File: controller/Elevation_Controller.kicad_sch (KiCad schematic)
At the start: 0 parts

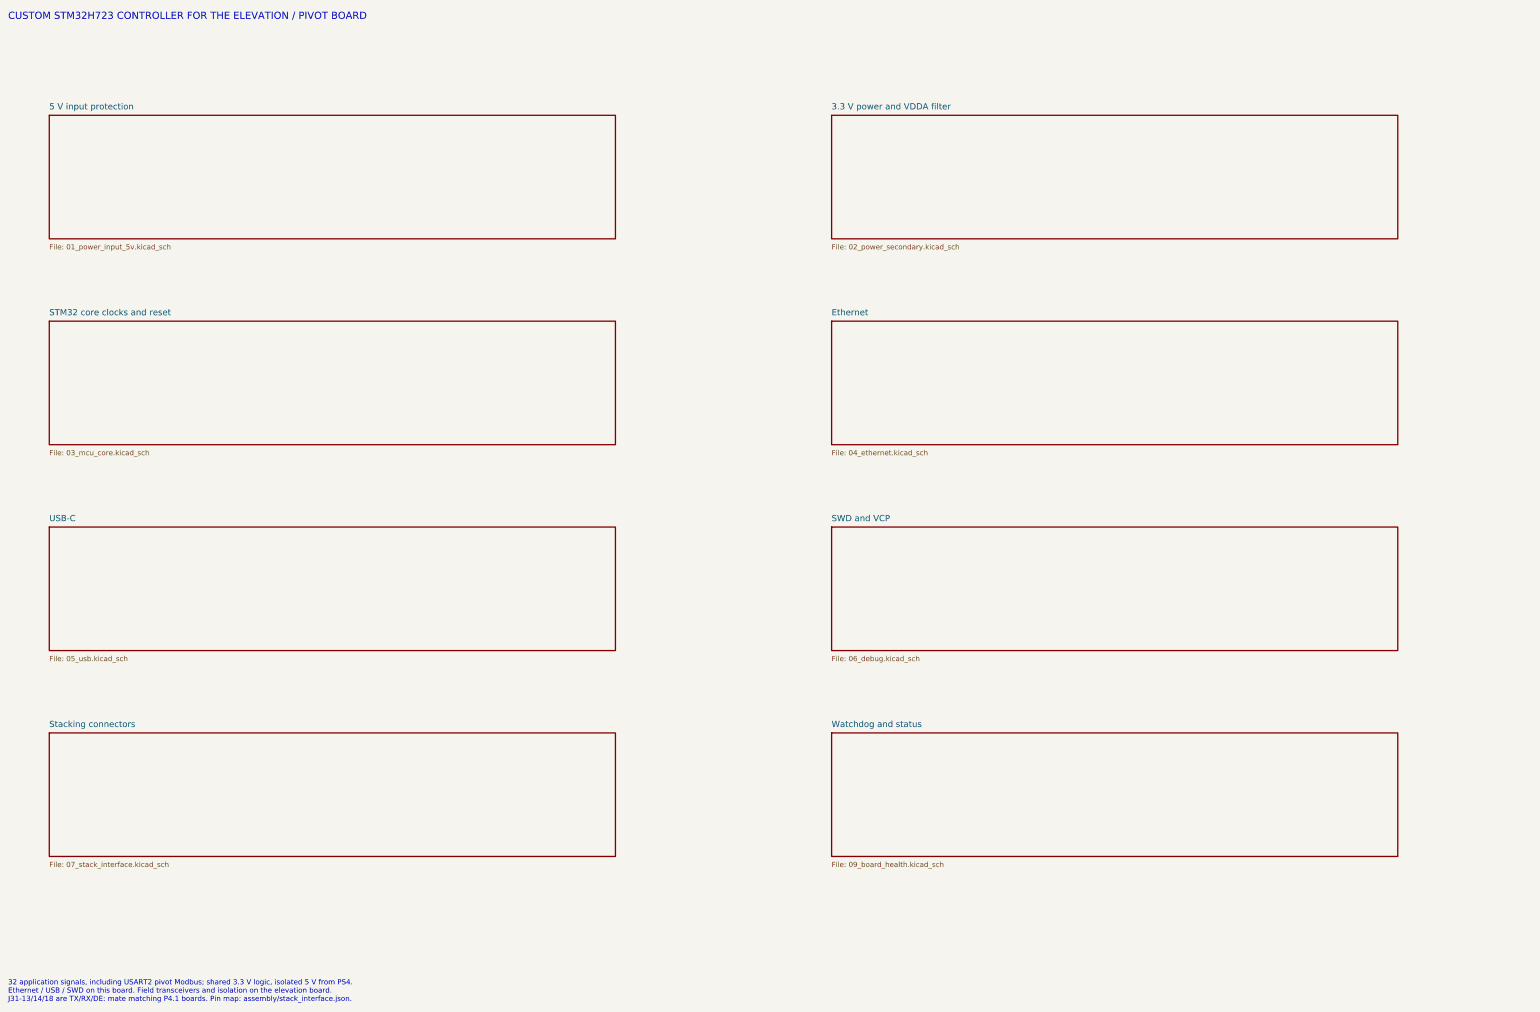
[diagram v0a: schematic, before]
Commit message: Build P6 80x130 stack with redistributed SSI and stepper interfaces
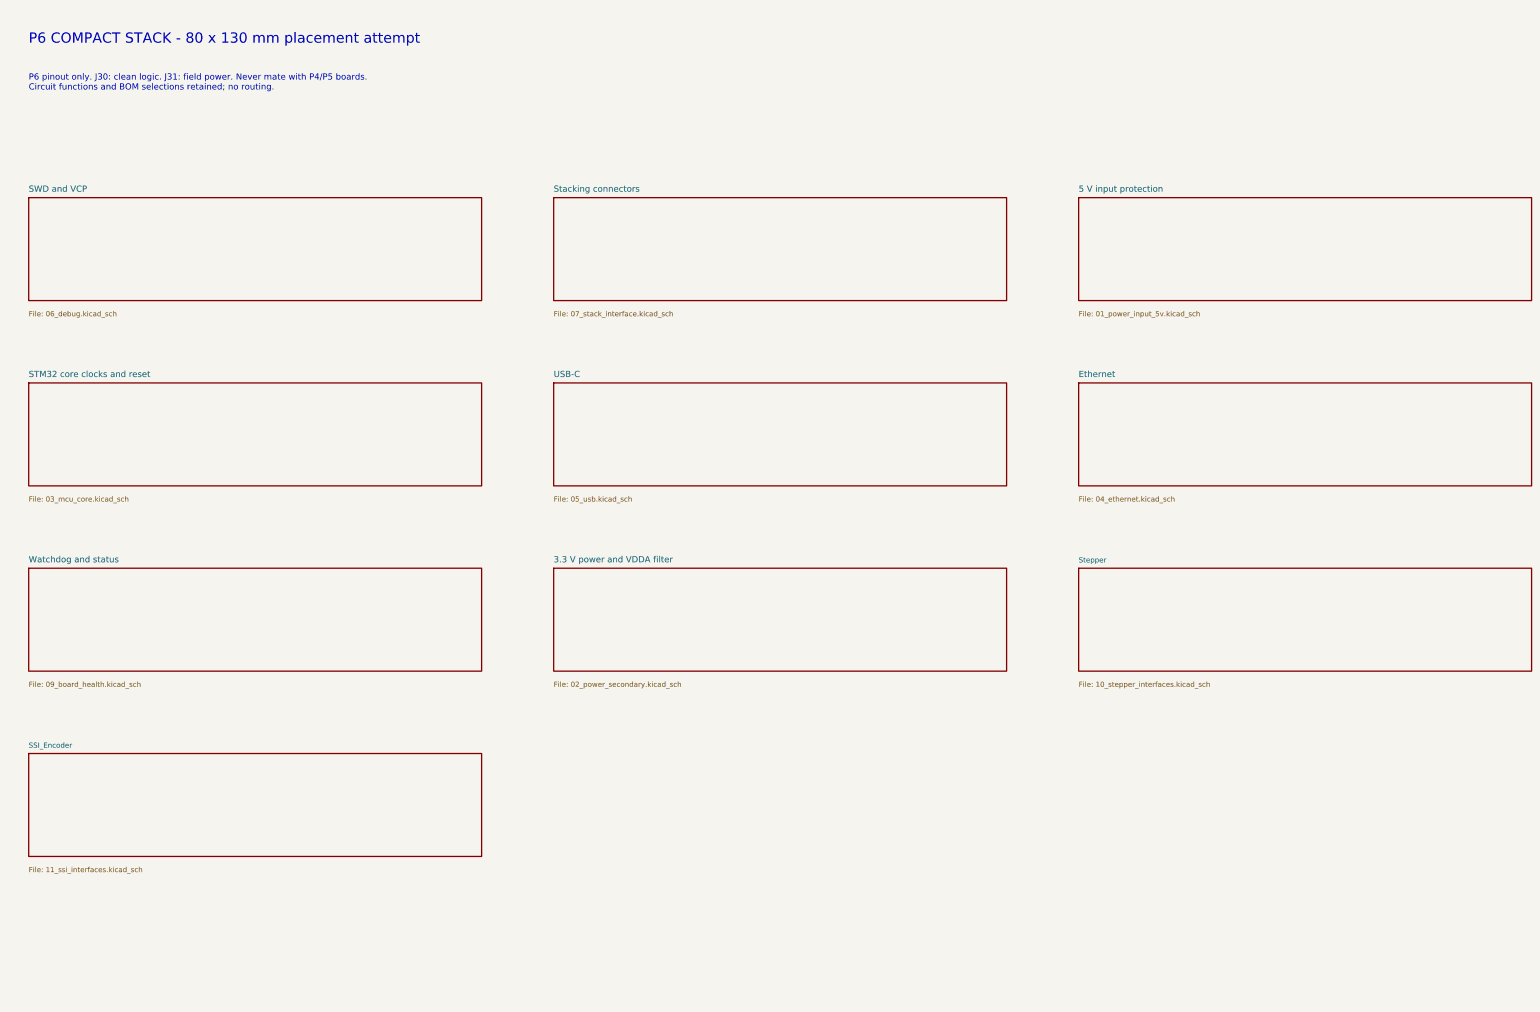
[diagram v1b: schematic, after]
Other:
- added sheet SSI_Encoder (11_ssi_interfaces.kicad_sch)
- added sheet Stepper (10_stepper_interfaces.kicad_sch)
- note added: "P6 COMPACT STACK - 80 x 130 mm placement attempt"
- note added: "P6 pinout only. J30: clean logic. J31: field power. Never mate with P4/P5 boards. Circuit functions and BOM selections retained; no routing."
- note removed: "32 application signals, including USART2 pivot Modbus; shared 3.3 V logic, isolated 5 V from PS4. Ethernet / USB / SWD on this board. Field transceivers and isolation on the elevation board. J31-13/14/18 are TX/RX/DE: mate matching P4.1 boards. Pin map: assembly/stack_interface.json."
- note removed: "CUSTOM STM32H723 CONTROLLER FOR THE ELEVATION / PIVOT BOARD"
